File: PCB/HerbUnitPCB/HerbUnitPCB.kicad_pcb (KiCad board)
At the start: 2 copper layers, 43 parts, among them J1 USB_C_Receptacle_USB2.0_16P, J2 Barrel_Jack_Switch_Pin3Ring, J3 Conn_01x03_Pin, J4 SD_Card_Device, J5 Screw_Terminal_01x02, J6 Conn_01x03_Pin, SW1 SW_Push, SW2 SW_Push, SW3 SW_Push, U1 USBLC6-2P6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

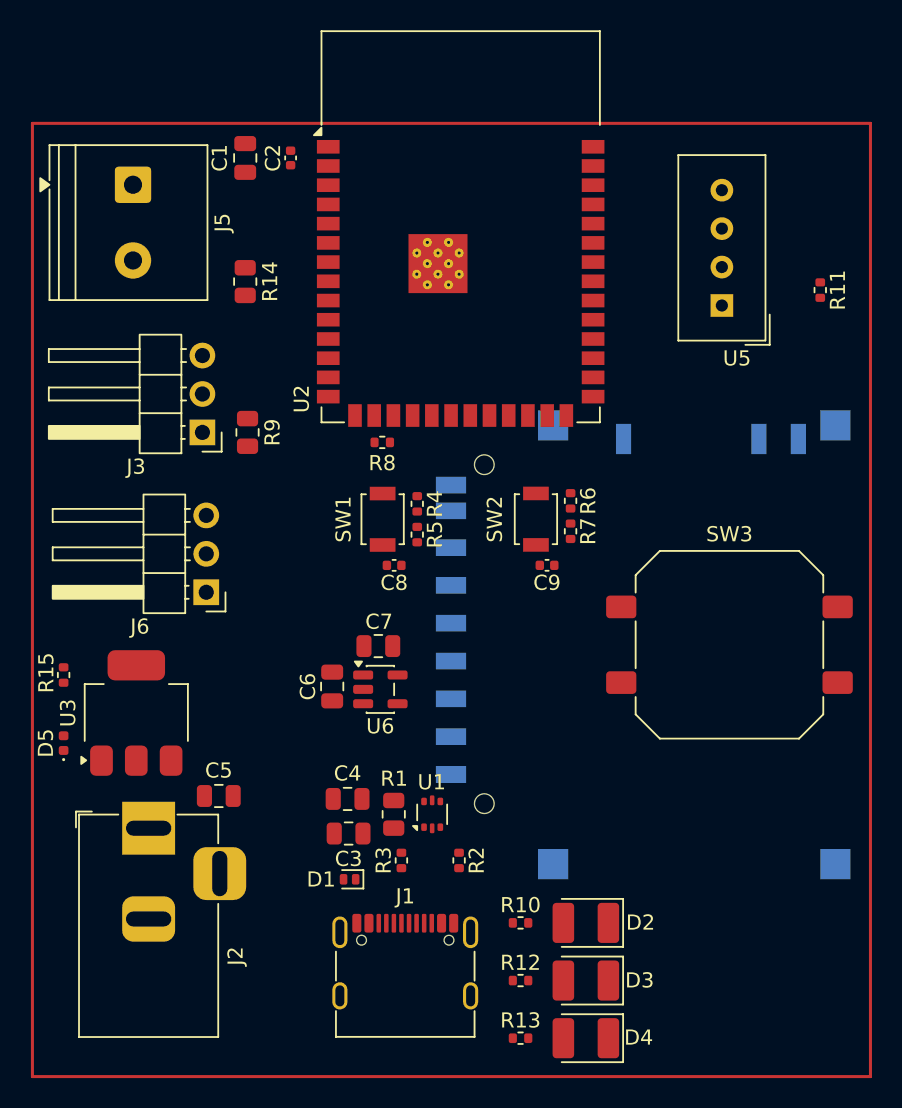
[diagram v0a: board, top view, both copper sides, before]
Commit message: OCD-Friendly Layout
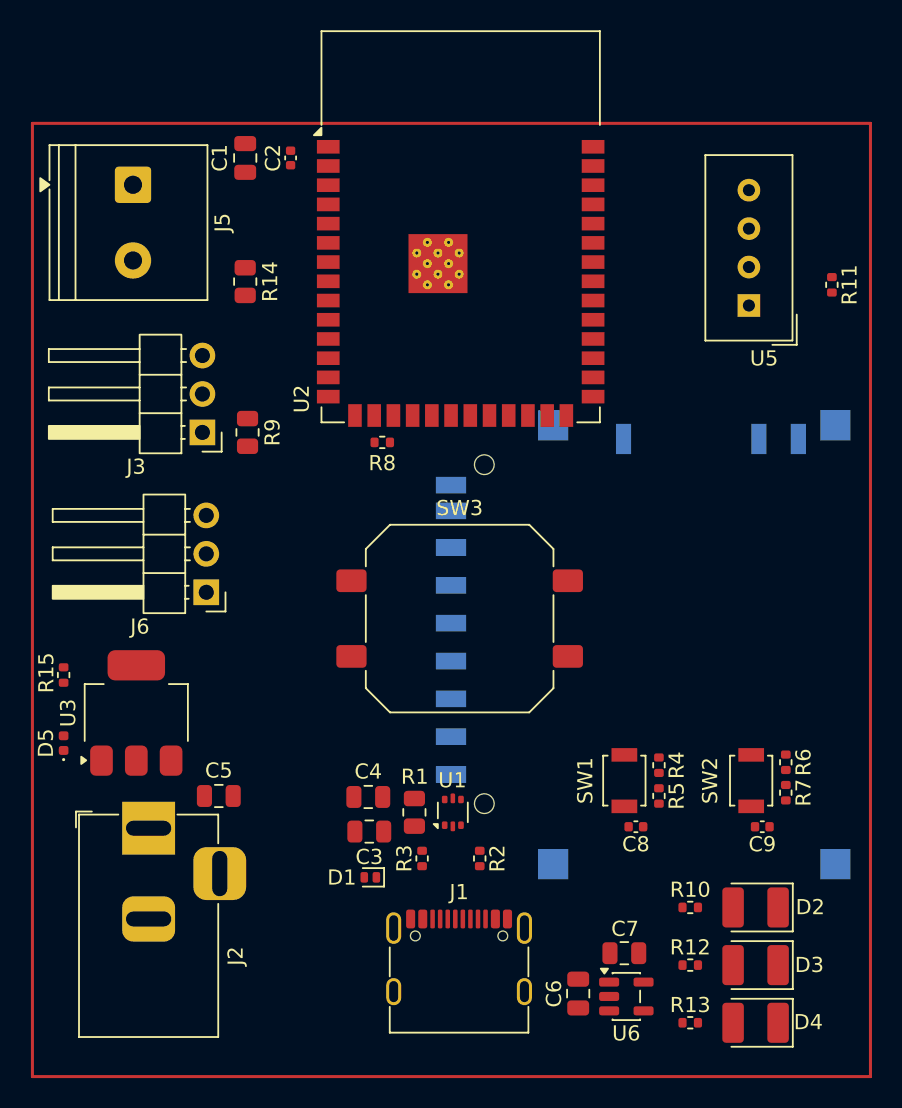
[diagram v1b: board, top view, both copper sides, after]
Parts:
- moved C7 26.0 mm to (178.1, 89.4)
- moved U6 26.0 mm to (178.2, 92.2)
- moved C6 26.0 mm to (175.0, 92.1)
- moved R5 23.5 mm to (180.3, 79.0)
- moved C8 23.5 mm to (178.8, 81.0)
- moved R4 23.5 mm to (180.3, 77.0)
- moved SW1 23.5 mm to (178.1, 78.0)
- moved SW2 22.4 mm to (186.4, 78.0)
- moved R6 22.4 mm to (188.7, 76.8)
- moved C9 22.4 mm to (187.2, 81.0)
- moved R7 22.4 mm to (188.7, 78.8)
- moved SW3 17.9 mm to (167.2, 67.3)
- moved D2 11.3 mm to (186.7, 86.4)
- moved D3 11.3 mm to (186.7, 90.2)
- moved D4 11.3 mm to (186.7, 94.0)
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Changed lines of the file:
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@@
 	(footprint "Capacitor_SMD:C_0805_2012Metric"
 		(layer "F.Cu")
-		(at 159.832 81.475 180)
+		(at 161.198 81.345 180)
 		(descr "Capacitor SMD 0805 (2012 Metric), square (rectangular) end terminal, IPC-7351 nominal, (Body size source: IPC-SM-782 page 76, https://www.pcb-3d.com/wordpress/wp-content/uploads/ipc-sm-782a_amendment_1_and_2.pdf, https://docs.google.com/spreadsheets/d/1BsfQQcO9C6DZCsRaXUlFlo91Tg2WpOkGARC1WS5S8t0/edit?usp=sharing)")
 		(tags "capacitor")
@@
 	(footprint "LED_SMD:LED_1210_3225Metric_Pad1.42x2.65mm_HandSolder"
 		(layer "F.Cu")
-		(at 175.5125 87.38 180)
+		(at 186.7265 86.36 180)
 		(descr "LED SMD 1210 (3225 Metric), square (rectangular) end terminal, IPC-7351 nominal, (Body size source: http://www.tortai-tech.com/upload/download/2011102023233369053.pdf)")
 		(tags "LED handsolder")
@@
 	(footprint "Diode_SMD:D_SOD-882D"
 		(layer "F.Cu")
-		(at 159.9 84.5 180)
+		(at 161.266 84.37 180)
 		(descr "SOD-882D, DFN1006D-2, body 1.0 x 0.6 x 0.4mm, pitch 0.65mm, https://assets.nexperia.com/documents/package-information/SOD882D.pdf")
 		(tags "Diode SOD882D DFN1006D-2")
@@
 	(footprint "Capacitor_SMD:C_0805_2012Metric"
 		(layer "F.Cu")
-		(at 161.798 69.088 180)
+		(at 178.054 89.382 180)
 		(descr "Capacitor SMD 0805 (2012 Metric), square (rectangular) end terminal, IPC-7351 nominal, (Body size source: IPC-SM-782 page 76, https://www.pcb-3d.com/wordpress/wp-content/uploads/ipc-sm-782a_amendment_1_and_2.pdf, https://docs.google.com/spreadsheets/d/1BsfQQcO9C6DZCsRaXUlFlo91Tg2WpOkGARC1WS5S8t0/edit?usp=sharing)")
 		(tags "capacitor")
@@
 	(footprint "Resistor_SMD:R_0402_1005Metric"
 		(layer "F.Cu")
-		(at 171.1945 87.38)
+		(at 182.4085 86.36)
 		(descr "Resistor SMD 0402 (1005 Metric), square (rectangular) end terminal, IPC-7351 nominal, (Body size source: IPC-SM-782 page 72, https://www.pcb-3d.com/wordpress/wp-content/uploads/ipc-sm-782a_amendment_1_and_2.pdf)")
 		(tags "resistor")
@@
 	(footprint "Resistor_SMD:R_0402_1005Metric"
 		(layer "F.Cu")
-		(at 191 45.562 -90)
+		(at 191.77 45.214 -90)
 		(descr "Resistor SMD 0402 (1005 Metric), square (rectangular) end terminal, IPC-7351 nominal, (Body size source: IPC-SM-782 page 72, https://www.pcb-3d.com/wordpress/wp-content/uploads/ipc-sm-782a_amendment_1_and_2.pdf)")
 		(tags "resistor")
@@
 	(footprint "Sensor:Aosong_DHT11_5.5x12.0_P2.54mm"
 		(layer "F.Cu")
-		(at 184.5 46.58 180)
+		(at 186.286 46.58 180)
 		(descr "Temperature and humidity module, http://akizukidenshi.com/download/ds/aosong/DHT11.pdf")
 		(tags "Temperature and humidity module")
@@
 	(footprint "Button_Switch_SMD:SW_SPST_B3U-1000P"
 		(layer "F.Cu")
-		(at 162.08 60.706 -90)
+		(at 178.054 77.978 -90)
 		(descr "Ultra-small-sized Tactile Switch with High Contact Reliability, Top-actuated Model, without Ground Terminal, without Boss")
 		(tags "Tactile Switch")
@@
 	(footprint "LED_SMD:LED_1210_3225Metric_Pad1.42x2.65mm_HandSolder"
 		(layer "F.Cu")
-		(at 175.5125 95 180)
+		(at 186.7265 93.98 180)
 		(descr "LED SMD 1210 (3225 Metric), square (rectangular) end terminal, IPC-7351 nominal, (Body size source: http://www.tortai-tech.com/upload/download/2011102023233369053.pdf)")
 		(tags "LED handsolder")
@@
 	(footprint "Connector_USB:USB_C_Receptacle_G-Switch_GT-USB-7010ASV"
 		(layer "F.Cu")
-		(at 163.576 91.127)
+		(at 167.132 90.847)
 		(descr "USB Type C, right-angle, SMT, https://datasheet.lcsc.com/lcsc/2204071530_G-Switch-GT-USB-7010ASV_C2988369.pdf")
 		(tags "USB C Type-C Receptacle SMD")
@@
 	(footprint "LED_SMD:LED_1210_3225Metric_Pad1.42x2.65mm_HandSolder"
 		(layer "F.Cu")
-		(at 175.5125 91.19 180)
+		(at 186.7265 90.17 180)
 		(descr "LED SMD 1210 (3225 Metric), square (rectangular) end terminal, IPC-7351 nominal, (Body size source: http://www.tortai-tech.com/upload/download/2011102023233369053.pdf)")
 		(tags "LED handsolder")
@@
 	(footprint "Resistor_SMD:R_0402_1005Metric"
 		(layer "F.Cu")
-		(at 163.322 83.253 90)
+		(at 164.688 83.123 90)
 		(descr "Resistor SMD 0402 (1005 Metric), square (rectangular) end terminal, IPC-7351 nominal, (Body size source: IPC-SM-782 page 72, https://www.pcb-3d.com/wordpress/wp-content/uploads/ipc-sm-782a_amendment_1_and_2.pdf)")
 		(tags "resistor")
@@
 	(footprint "Capacitor_SMD:C_0805_2012Metric"
 		(layer "F.Cu")
-		(at 158.748 71.757 -90)
+		(at 175.004 92.051 -90)
 		(descr "Capacitor SMD 0805 (2012 Metric), square (rectangular) end terminal, IPC-7351 nominal, (Body size source: IPC-SM-782 page 76, https://www.pcb-3d.com/wordpress/wp-content/uploads/ipc-sm-782a_amendment_1_and_2.pdf, https://docs.google.com/spreadsheets/d/1BsfQQcO9C6DZCsRaXUlFlo91Tg2WpOkGARC1WS5S8t0/edit?usp=sharing)")
 		(tags "capacitor")
@@
 	(footprint "Resistor_SMD:R_0402_1005Metric"
 		(layer "F.Cu")
-		(at 164.366 61.72 -90)
+		(at 180.34 78.992 -90)
 		(descr "Resistor SMD 0402 (1005 Metric), square (rectangular) end terminal, IPC-7351 nominal, (Body size source: IPC-SM-782 page 72, https://www.pcb-3d.com/wordpress/wp-content/uploads/ipc-sm-782a_amendment_1_and_2.pdf)")
 		(tags "resistor")
@@
 	(footprint "Button_Switch_SMD:SW_SPST_B3U-1000P"
 		(layer "F.Cu")
-		(at 172.212 60.702 -90)
+		(at 186.436 77.978 -90)
 		(descr "Ultra-small-sized Tactile Switch with High Contact Reliability, Top-actuated Model, without Ground Terminal, without Boss")
 		(tags "Tactile Switch")
@@
 	(footprint "Resistor_SMD:R_0402_1005Metric"
 		(layer "F.Cu")
-		(at 174.5 61.5 -90)
+		(at 188.724 78.776 -90)
 		(descr "Resistor SMD 0402 (1005 Metric), square (rectangular) end terminal, IPC-7351 nominal, (Body size source: IPC-SM-782 page 72, https://www.pcb-3d.com/wordpress/wp-content/uploads/ipc-sm-782a_amendment_1_and_2.pdf)")
 		(tags "resistor")
@@
 	(footprint "Resistor_SMD:R_0402_1005Metric"
 		(layer "F.Cu")
-		(at 171.1945 91.19)
+		(at 182.4085 90.17)
 		(descr "Resistor SMD 0402 (1005 Metric), square (rectangular) end terminal, IPC-7351 nominal, (Body size source: IPC-SM-782 page 72, https://www.pcb-3d.com/wordpress/wp-content/uploads/ipc-sm-782a_amendment_1_and_2.pdf)")
 		(tags "resistor")
@@
 	(footprint "Resistor_SMD:R_0402_1005Metric"
 		(layer "F.Cu")
-		(at 171.1945 95)
+		(at 182.4085 93.98)
 		(descr "Resistor SMD 0402 (1005 Metric), square (rectangular) end terminal, IPC-7351 nominal, (Body size source: IPC-SM-782 page 72, https://www.pcb-3d.com/wordpress/wp-content/uploads/ipc-sm-782a_amendment_1_and_2.pdf)")
 		(tags "resistor")
@@
 	(footprint "Resistor_SMD:R_0402_1005Metric"
 		(layer "F.Cu")
-		(at 164.366 59.688 -90)
+		(at 180.34 76.96 -90)
 		(descr "Resistor SMD 0402 (1005 Metric), square (rectangular) end terminal, IPC-7351 nominal, (Body size source: IPC-SM-782 page 72, https://www.pcb-3d.com/wordpress/wp-content/uploads/ipc-sm-782a_amendment_1_and_2.pdf)")
 		(tags "resistor")
@@
 	(footprint "Capacitor_SMD:C_0805_2012Metric"
 		(layer "F.Cu")
-		(at 159.766 79.189)
+		(at 161.132 79.059)
 		(descr "Capacitor SMD 0805 (2012 Metric), square (rectangular) end terminal, IPC-7351 nominal, (Body size source: IPC-SM-782 page 76, https://www.pcb-3d.com/wordpress/wp-content/uploads/ipc-sm-782a_amendment_1_and_2.pdf, https://docs.google.com/spreadsheets/d/1BsfQQcO9C6DZCsRaXUlFlo91Tg2WpOkGARC1WS5S8t0/edit?usp=sharing)")
 		(tags "capacitor")
@@
 	(footprint "Package_TO_SOT_SMD:SOT-23-5"
 		(layer "F.Cu")
-		(at 161.9305 71.948)
+		(at 178.1865 92.242)
 		(descr "SOT, 5 Pin (JEDEC MO-178 Var AA https://www.jedec.org/document_search?search_api_views_fulltext=MO-178)")
 		(tags "SOT TO_SOT_SMD")
@@
 	(footprint "Resistor_SMD:R_0805_2012Metric"
 		(layer "F.Cu")
-		(at 162.814 80.205 90)
+		(at 164.18 80.075 90)
 		(descr "Resistor SMD 0805 (2012 Metric), square (rectangular) end terminal, IPC-7351 nominal, (Body size source: IPC-SM-782 page 72, https://www.pcb-3d.com/wordpress/wp-content/uploads/ipc-sm-782a_amendment_1_and_2.pdf)")
 		(tags "resistor")
@@
 	(footprint "Resistor_SMD:R_0402_1005Metric"
 		(layer "F.Cu")
-		(at 174.5 59.49 -90)
+		(at 188.724 76.766 -90)
 		(descr "Resistor SMD 0402 (1005 Metric), square (rectangular) end terminal, IPC-7351 nominal, (Body size source: IPC-SM-782 page 72, https://www.pcb-3d.com/wordpress/wp-content/uploads/ipc-sm-782a_amendment_1_and_2.pdf)")
 		(tags "resistor")
@@
 	(footprint "Capacitor_SMD:C_0402_1005Metric"
 		(layer "F.Cu")
-		(at 162.842 63.754 180)
+		(at 178.816 81.026 180)
 		(descr "Capacitor SMD 0402 (1005 Metric), square (rectangular) end terminal, IPC-7351 nominal, (Body size source: IPC-SM-782 page 76, https://www.pcb-3d.com/wordpress/wp-content/uploads/ipc-sm-782a_amendment_1_and_2.pdf)")
 		(tags "capacitor")
@@
 	(footprint "Package_TO_SOT_SMD:SOT-666"
 		(layer "F.Cu")
-		(at 165.354 80.205 90)
+		(at 166.72 80.075 90)
 		(descr "SOT666")
 		(tags "SOT-666")
@@
 	(footprint "Button_Switch_SMD:SW_Push_1P1T_NO_CK_PTS125Sx43SMTR"
 		(layer "F.Cu")
-		(at 185 69)
+		(at 167.17 67.27)
 		(descr "Tactile switch, 12x12 mm, H4.3 mm, round actuator, gullwing terminals, https://www.ckswitches.com/media/1462/pts125.pdf")
 		(tags "button tactile Switch SPST 1P1T C&K")
@@
 	(footprint "Resistor_SMD:R_0402_1005Metric"
 		(layer "F.Cu")
-		(at 167.132 83.253 -90)
+		(at 168.498 83.123 -90)
 		(descr "Resistor SMD 0402 (1005 Metric), square (rectangular) end terminal, IPC-7351 nominal, (Body size source: IPC-SM-782 page 72, https://www.pcb-3d.com/wordpress/wp-content/uploads/ipc-sm-782a_amendment_1_and_2.pdf)")
 		(tags "resistor")
@@
 	(footprint "Capacitor_SMD:C_0402_1005Metric"
 		(layer "F.Cu")
-		(at 172.946 63.75 180)
+		(at 187.17 81.026 180)
 		(descr "Capacitor SMD 0402 (1005 Metric), square (rectangular) end terminal, IPC-7351 nominal, (Body size source: IPC-SM-782 page 76, https://www.pcb-3d.com/wordpress/wp-content/uploads/ipc-sm-782a_amendment_1_and_2.pdf)")
 		(tags "capacitor")
@@
 		)
 		(fp_text user "${REFERENCE}"
-			(at 0 0 90)
+			(at 6.642 1.494 90)
 			(layer "B.Fab")
 			(effects
